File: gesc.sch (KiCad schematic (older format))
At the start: 34 parts, among them J1 Conn_01x06, J13 T-Motor, J15 EXT_OFF, J2 Conn_01x06, J3 Conn_01x06, J4 Conn_01x05, J5 Conn_01x03, J6 USB_B_Mini, J7 BAT+, J8 BAT-

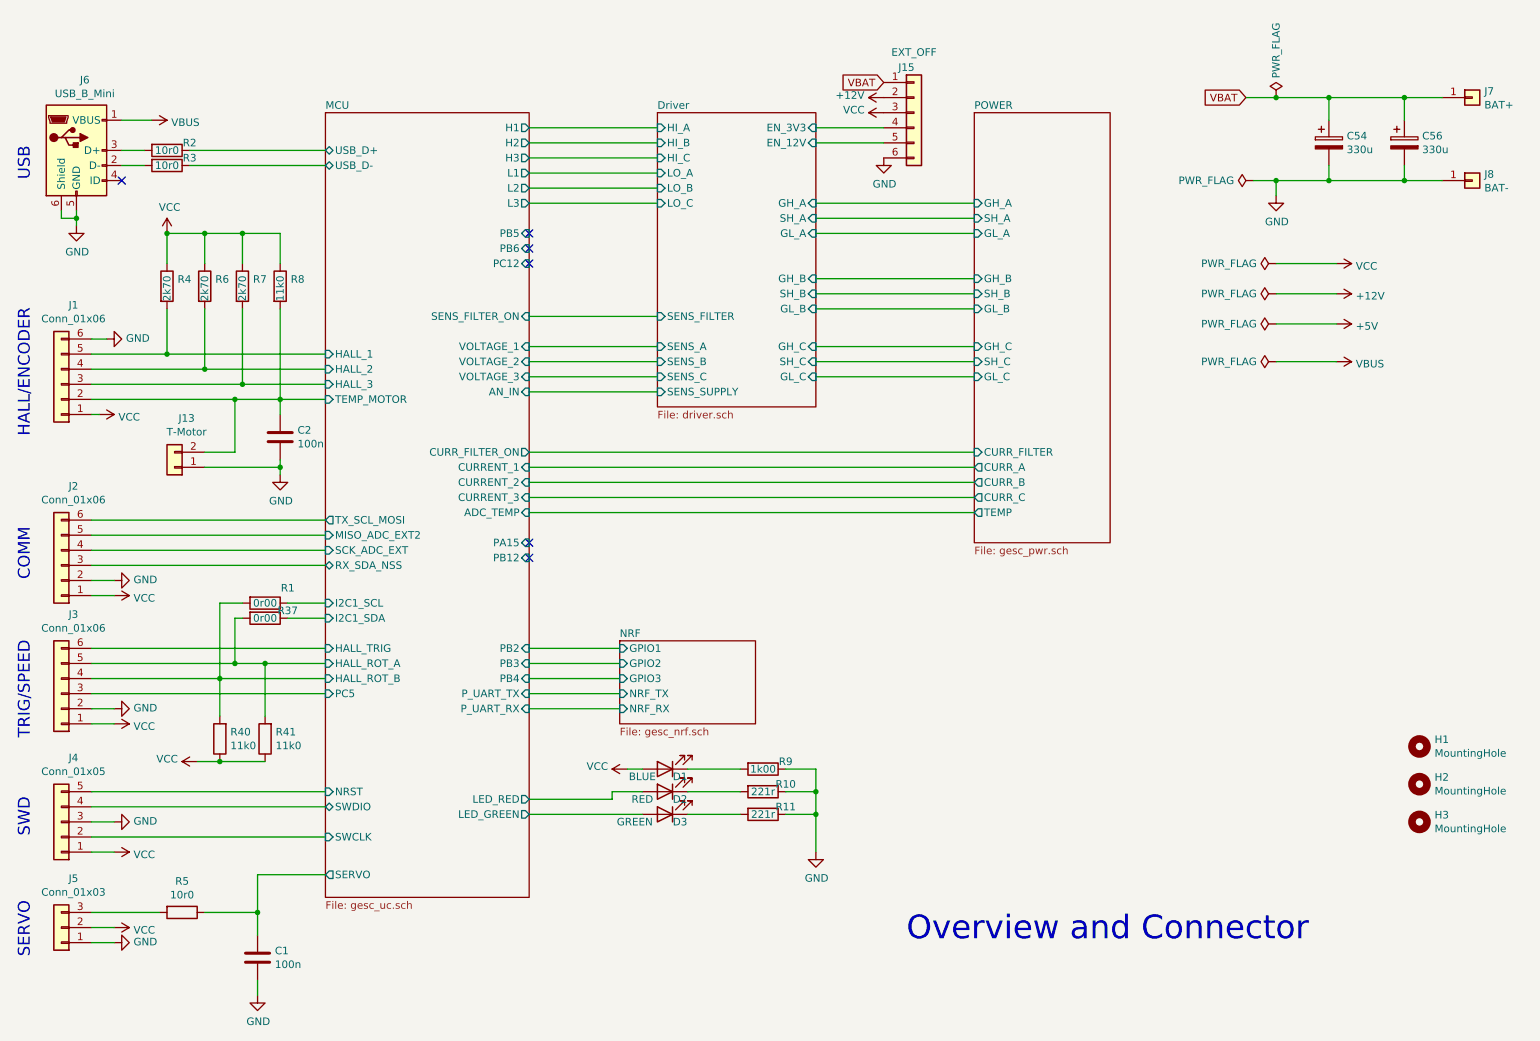
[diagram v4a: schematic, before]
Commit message: - new driver 2ED2304S06F - separat Elkos for each phase - new FET placement
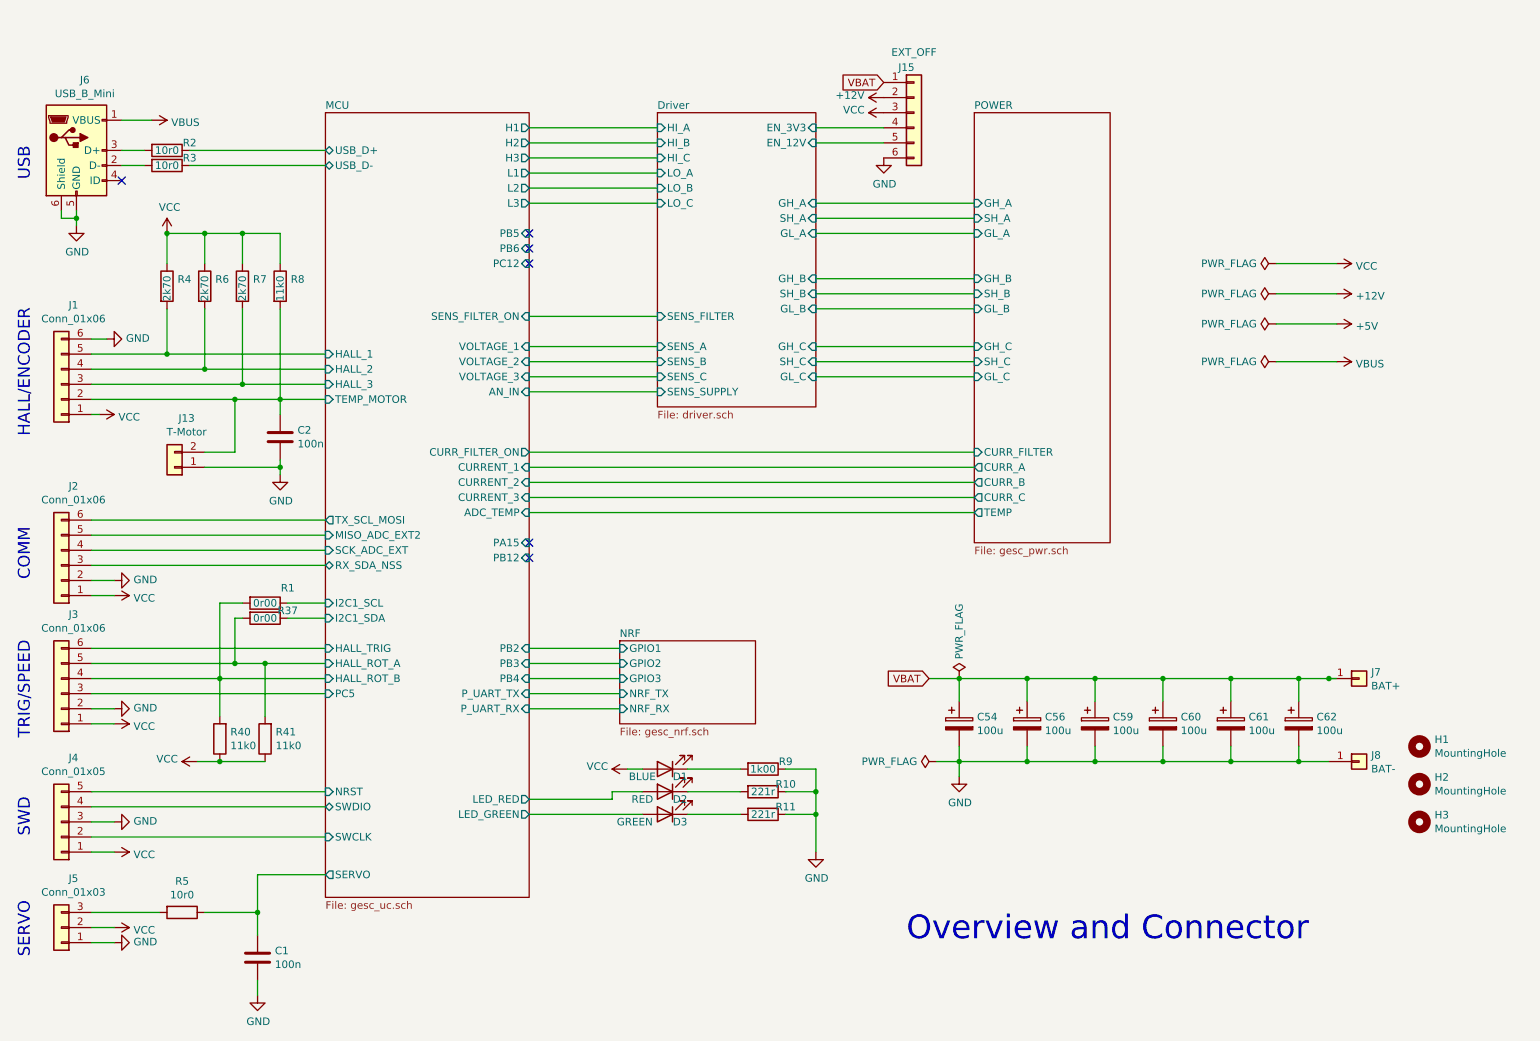
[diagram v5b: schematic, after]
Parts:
- added C59, C60, C61, C62: 100u, Capacitor_SMD:CP_Elec_10x10, symbol Device:CP
- C54, C56: value 330u -> 100u; footprint Capacitor_SMD:CP_Elec_16x17.5 -> Capacitor_SMD:CP_Elec_10x10
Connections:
- net GND: now also C59.2, C60.2, C61.2, C62.2
- net VBAT: now also C59.1, C60.1, C61.1, C62.1
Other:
- moved on the sheet: C54, C56, J7, J8
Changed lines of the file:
@@
 L Connector_Generic:Conn_01x01 J7
 U 1 1 5C0450D0
-P 10850 1350
-F 0 "J7" H 10930 1392 50  0000 L CNN
-F 1 "BAT+" H 10930 1301 50  0000 L CNN
-F 2 "gesc:TestPoint_Pad_5.0x5.0mm" H 10850 1350 50  0001 C CNN
-F 3 "~" H 10850 1350 50  0001 C CNN
-	1    10850 1350
+P 10100 5200
+F 0 "J7" H 10180 5242 50  0000 L CNN
+F 1 "BAT+" H 10180 5151 50  0000 L CNN
+F 2 "gesc:TestPoint_Pad_5.0x5.0mm" H 10100 5200 50  0001 C CNN
+F 3 "~" H 10100 5200 50  0001 C CNN
+	1    10100 5200
 	1    0    0    -1
 $EndComp
@@
 L Connector_Generic:Conn_01x01 J8
 U 1 1 5C045122
-P 10850 1900
-F 0 "J8" H 10930 1942 50  0000 L CNN
-F 1 "BAT-" H 10930 1851 50  0000 L CNN
-F 2 "gesc:TestPoint_Pad_5.0x5.0mm" H 10850 1900 50  0001 C CNN
-F 3 "~" H 10850 1900 50  0001 C CNN
-	1    10850 1900
+P 10100 5750
+F 0 "J8" H 10180 5792 50  0000 L CNN
+F 1 "BAT-" H 10180 5701 50  0000 L CNN
+F 2 "gesc:TestPoint_Pad_5.0x5.0mm" H 10100 5750 50  0001 C CNN
+F 3 "~" H 10100 5750 50  0001 C CNN
+	1    10100 5750
 	1    0    0    -1
 $EndComp
@@
 L power:GND #PWR019
 U 1 1 5C04D5C9
-P 9550 2000
-F 0 "#PWR019" H 9550 1750 50  0001 C CNN
-F 1 "GND" H 9555 1827 50  0000 C CNN
-F 2 "" H 9550 2000 50  0001 C CNN
-F 3 "" H 9550 2000 50  0001 C CNN
-	1    9550 2000
+P 7450 5850
+F 0 "#PWR019" H 7450 5600 50  0001 C CNN
+F 1 "GND" H 7455 5677 50  0000 C CNN
+F 2 "" H 7450 5850 50  0001 C CNN
+F 3 "" H 7450 5850 50  0001 C CNN
+	1    7450 5850
 	1    0    0    -1
 $EndComp
@@
 L power:PWR_FLAG #FLG0102
 U 1 1 5C34D8D2
-P 9550 1350
-F 0 "#FLG0102" H 9550 1425 50  0001 C CNN
-F 1 "PWR_FLAG" V 9550 1478 50  0000 L CNN
-F 2 "" H 9550 1350 50  0001 C CNN
-F 3 "~" H 9550 1350 50  0001 C CNN
-	1    9550 1350
+P 7450 5200
+F 0 "#FLG0102" H 7450 5275 50  0001 C CNN
+F 1 "PWR_FLAG" V 7450 5328 50  0000 L CNN
+F 2 "" H 7450 5200 50  0001 C CNN
+F 3 "~" H 7450 5200 50  0001 C CNN
+	1    7450 5200
 	1    0    0    -1
 $EndComp
@@
 F15 "CURR_FILTER" I L 7550 3700 50
 $EndSheet
-Text GLabel 9350 1350 0    50   Input ~ 0
+Text GLabel 7250 5200 0    50   Input ~ 0
 VBAT
 Wire Wire Line
-	9550 1900 9550 2000
+	7450 5750 7450 5850
 Wire Wire Line
 	9550 2450 9950 2450
@@
 L power:PWR_FLAG #FLG0103
 U 1 1 5E9A74C6
-P 9400 1900
-F 0 "#FLG0103" H 9400 1975 50  0001 C CNN
-F 1 "PWR_FLAG" V 9400 2028 50  0000 L CNN
-F 2 "" H 9400 1900 50  0001 C CNN
-F 3 "~" H 9400 1900 50  0001 C CNN
-	1    9400 1900
+P 7300 5750
+F 0 "#FLG0103" H 7300 5825 50  0001 C CNN
+F 1 "PWR_FLAG" V 7300 5878 50  0000 L CNN
+F 2 "" H 7300 5750 50  0001 C CNN
+F 3 "~" H 7300 5750 50  0001 C CNN
+	1    7300 5750
 	0    -1   -1   0
 $EndComp
@@
 	0    -1   -1   0
 $EndComp
-Connection ~ 9550 1900
-$Comp
-L Device:CP C54
-U 1 1 5F3843DA
-P 9900 1650
-F 0 "C54" H 10018 1696 50  0000 L CNN
-F 1 "330u" H 10018 1605 50  0000 L CNN
-F 2 "Capacitor_SMD:CP_Elec_16x17.5" H 9938 1500 50  0001 C CNN
-F 3 "~" H 9900 1650 50  0001 C CNN
-	1    9900 1650
-	1    0    0    -1
-$EndComp
-Wire Wire Line
-	9900 1800 9900 1900
-Wire Wire Line
-	9900 1500 9900 1350
-Wire Wire Line
-	9350 1350 9550 1350
-Connection ~ 9900 1350
-Connection ~ 9550 1350
-$Comp
-L Device:CP C56
-U 1 1 5F3B3A4A
-P 10400 1650
-F 0 "C56" H 10518 1696 50  0000 L CNN
-F 1 "330u" H 10518 1605 50  0000 L CNN
-F 2 "Capacitor_SMD:CP_Elec_16x17.5" H 10438 1500 50  0001 C CNN
-F 3 "~" H 10400 1650 50  0001 C CNN
-	1    10400 1650
-	1    0    0    -1
-$EndComp
-Wire Wire Line
-	10400 1800 10400 1900
-Wire Wire Line
-	10400 1500 10400 1350
-Wire Wire Line
-	10400 1350 10650 1350
-Wire Wire Line
-	10400 1900 10650 1900
+Connection ~ 7450 5750
+Wire Wire Line
+	7450 5650 7450 5750
+Wire Wire Line
+	7450 5350 7450 5200
+Wire Wire Line
+	7250 5200 7450 5200
+Connection ~ 7450 5200
+Wire Wire Line
+	7900 5650 7900 5750
 Wire Wire Line
 	3250 4700 3000 4700
@@
 	2550 5200 3250 5200
 Wire Wire Line
-	9550 1350 9900 1350
-Wire Wire Line
-	9550 1900 9900 1900
-Wire Wire Line
-	9900 1350 10400 1350
-Connection ~ 10400 1350
-Wire Wire Line
-	9900 1900 10400 1900
-Connection ~ 9900 1900
-Connection ~ 10400 1900
-Wire Wire Line
-	9400 1900 9550 1900
+	7300 5750 7450 5750
 $Comp
 L Device:R R40
@@
 	0    1    1    0
 $EndComp
+$Comp
+L Device:CP C54
+U 1 1 5F3843DA
+P 7450 5500
+F 0 "C54" H 7568 5546 50  0000 L CNN
+F 1 "100u" H 7568 5455 50  0000 L CNN
+F 2 "Capacitor_SMD:CP_Elec_10x10" H 7488 5350 50  0001 C CNN
+F 3 "~" H 7450 5500 50  0001 C CNN
+	1    7450 5500
+	1    0    0    -1
+$EndComp
+$Comp
+L Device:CP C56
+U 1 1 5F3B3A4A
+P 7900 5500
+F 0 "C56" H 8018 5546 50  0000 L CNN
+F 1 "100u" H 8018 5455 50  0000 L CNN
+F 2 "Capacitor_SMD:CP_Elec_10x10" H 7938 5350 50  0001 C CNN
+F 3 "~" H 7900 5500 50  0001 C CNN
+	1    7900 5500
+	1    0    0    -1
+$EndComp
+Wire Wire Line
+	7450 5750 7900 5750
+Connection ~ 7900 5750
+Wire Wire Line
+	8350 5650 8350 5750
+Wire Wire Line
+	8350 5350 8350 5200
+Wire Wire Line
+	8800 5650 8800 5750
+Wire Wire Line
+	8800 5350 8800 5200
+$Comp
+L Device:CP C59
+U 1 1 6065ADC7
+P 8350 5500
+F 0 "C59" H 8468 5546 50  0000 L CNN
+F 1 "100u" H 8468 5455 50  0000 L CNN
+F 2 "Capacitor_SMD:CP_Elec_10x10" H 8388 5350 50  0001 C CNN
+F 3 "~" H 8350 5500 50  0001 C CNN
+	1    8350 5500
+	1    0    0    -1
+$EndComp
+$Comp
+L Device:CP C60
+U 1 1 6065ADD1
+P 8800 5500
+F 0 "C60" H 8918 5546 50  0000 L CNN
+F 1 "100u" H 8918 5455 50  0000 L CNN
+F 2 "Capacitor_SMD:CP_Elec_10x10" H 8838 5350 50  0001 C CNN
+F 3 "~" H 8800 5500 50  0001 C CNN
+	1    8800 5500
+	1    0    0    -1
+$EndComp
+Wire Wire Line
+	8350 5200 8800 5200
+Connection ~ 8800 5200
+Wire Wire Line
+	8800 5200 9250 5200
+Connection ~ 8350 5750
+Connection ~ 8800 5750
+Wire Wire Line
+	8800 5750 9250 5750
+Connection ~ 9900 5200
+Wire Wire Line
+	9900 5200 9950 5200
+Wire Wire Line
+	7900 5750 8350 5750
+Wire Wire Line
+	8350 5750 8800 5750
+Wire Wire Line
+	9250 5650 9250 5750
+Wire Wire Line
+	9250 5350 9250 5200
+Wire Wire Line
+	9700 5650 9700 5750
+Wire Wire Line
+	9700 5350 9700 5200
+$Comp
+L Device:CP C61
+U 1 1 6066BE77
+P 9250 5500
+F 0 "C61" H 9368 5546 50  0000 L CNN
+F 1 "100u" H 9368 5455 50  0000 L CNN
+F 2 "Capacitor_SMD:CP_Elec_10x10" H 9288 5350 50  0001 C CNN
+F 3 "~" H 9250 5500 50  0001 C CNN
+	1    9250 5500
+	1    0    0    -1
+$EndComp
+$Comp
+L Device:CP C62
+U 1 1 6066BE81
+P 9700 5500
+F 0 "C62" H 9818 5546 50  0000 L CNN
+F 1 "100u" H 9818 5455 50  0000 L CNN
+F 2 "Capacitor_SMD:CP_Elec_10x10" H 9738 5350 50  0001 C CNN
+F 3 "~" H 9700 5500 50  0001 C CNN
+	1    9700 5500
+	1    0    0    -1
+$EndComp
+Connection ~ 9250 5200
+Wire Wire Line
+	9250 5200 9700 5200
+Connection ~ 9250 5750
+Wire Wire Line
+	9250 5750 9700 5750
+Connection ~ 9700 5200
+Wire Wire Line
+	9700 5200 9900 5200
+Connection ~ 9700 5750
+Wire Wire Line
+	9700 5750 9900 5750
+Connection ~ 8350 5200
+Wire Wire Line
+	7900 5200 8350 5200
+Wire Wire Line
+	7450 5200 7900 5200
+Wire Wire Line
+	7900 5350 7900 5200
+Connection ~ 7900 5200
 $EndSCHEMATC

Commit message: save
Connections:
- net Driver/EN_3V3 renamed Driver/V_AUX
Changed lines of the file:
@@
 F20 "SENS_B" I L 5450 3100 50
 F21 "SENS_A" I L 5450 3000 50
-F22 "EN_3V3" I R 6500 1550 50
-F23 "EN_12V" I R 6500 1650 50
+F22 "EN_12V" I R 6500 1650 50
+F23 "V_AUX" I R 6500 1550 50
 $EndSheet
 Wire Wire Line
@@
 NoConn ~ 4600 2350
 NoConn ~ 4600 2450
-Wire Wire Line
-	6500 1550 6950 1550
 $Comp
 L Connector_Generic:Conn_01x06 J15
@@
 	7900 5350 7900 5200
 Connection ~ 7900 5200
+Wire Wire Line
+	6500 1550 6950 1550
 $EndSCHEMATC

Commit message: save
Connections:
- net VBUS: no longer J6.1 (VBUS)
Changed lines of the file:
@@
 	2400 5750 2550 5750
 Connection ~ 2550 5750
-Wire Wire Line
-	1900 1500 2100 1500
 $Comp
 L power:PWR_FLAG #FLG0106
@@
 	0    1    1    0
 $EndComp
-$Comp
-L power:VBUS #PWR0150
-U 1 1 6015E336
-P 2100 1500
-F 0 "#PWR0150" H 2100 1350 50  0001 C CNN
-F 1 "VBUS" V 2115 1628 50  0000 L CNN
-F 2 "" H 2100 1500 50  0001 C CNN
-F 3 "" H 2100 1500 50  0001 C CNN
-	1    2100 1500
-	0    1    1    0
-$EndComp
